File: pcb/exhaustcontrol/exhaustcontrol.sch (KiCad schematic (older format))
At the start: 17 parts, among them J1 Conn_01x03, J2 Conn_01x02, Q1 BC547, U1 74LS08

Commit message: Final fixes.
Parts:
- R1: value 5k6 -> 0R
- R2: value 1k -> 4k7
- U1: value 74LS08 -> 74HC08
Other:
- note added: "J7:5"
- note removed: "HEATER"
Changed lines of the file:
@@
 EESchema Schematic File Version 4
-LIBS:exhaustcontrol-cache
 EELAYER 30 0
 EELAYER END
@@
 P 2850 2600
 F 0 "U1" H 2850 2925 50  0000 C CNN
-F 1 "74LS08" H 2850 2834 50  0000 C CNN
+F 1 "74HC08" H 2850 2834 50  0000 C CNN
 F 2 "Package_DIP:DIP-14_W7.62mm_LongPads" H 2850 2600 50  0001 C CNN
 F 3 "http://www.ti.com/lit/gpn/sn74LS08" H 2850 2600 50  0001 C CNN
@@
 P 2300 2300
 F 0 "R1" H 2370 2346 50  0000 L CNN
-F 1 "5k6" H 2370 2255 50  0000 L CNN
+F 1 "0R" H 2370 2255 50  0000 L CNN
 F 2 "Resistor_THT:R_Axial_DIN0411_L9.9mm_D3.6mm_P12.70mm_Horizontal" V 2230 2300 50  0001 C CNN
 F 3 "~" H 2300 2300 50  0001 C CNN
@@
 P 2300 2900
 F 0 "R2" H 2370 2946 50  0000 L CNN
-F 1 "1k" H 2370 2855 50  0000 L CNN
+F 1 "4k7" H 2370 2855 50  0000 L CNN
 F 2 "Resistor_THT:R_Axial_DIN0411_L9.9mm_D3.6mm_P12.70mm_Horizontal" V 2230 2900 50  0001 C CNN
 F 3 "~" H 2300 2900 50  0001 C CNN
@@
 P 5300 2600
 F 0 "U1" H 5300 2925 50  0000 C CNN
-F 1 "74LS08" H 5300 2834 50  0000 C CNN
+F 1 "74HC08" H 5300 2834 50  0000 C CNN
 F 2 "Package_DIP:DIP-14_W7.62mm_LongPads" H 5300 2600 50  0001 C CNN
 F 3 "http://www.ti.com/lit/gpn/sn74LS08" H 5300 2600 50  0001 C CNN
@@
 P 5900 4850
 F 0 "U1" H 5900 5175 50  0000 C CNN
-F 1 "74LS08" H 5900 5084 50  0000 C CNN
+F 1 "74HC08" H 5900 5084 50  0000 C CNN
 F 2 "Package_DIP:DIP-14_W7.62mm_LongPads" H 5900 4850 50  0001 C CNN
 F 3 "http://www.ti.com/lit/gpn/sn74LS08" H 5900 4850 50  0001 C CNN
@@
 P 4550 4850
 F 0 "U1" H 4550 5175 50  0000 C CNN
-F 1 "74LS08" H 4550 5084 50  0000 C CNN
+F 1 "74HC08" H 4550 5084 50  0000 C CNN
 F 2 "Package_DIP:DIP-14_W7.62mm_LongPads" H 4550 4850 50  0001 C CNN
 F 3 "http://www.ti.com/lit/gpn/sn74LS08" H 4550 4850 50  0001 C CNN
@@
 +5V
 Text Notes 1150 2150 0    50   ~ 0
-HEATER
+J7:5
 Text Notes 1150 2300 0    50   ~ 0
 GND

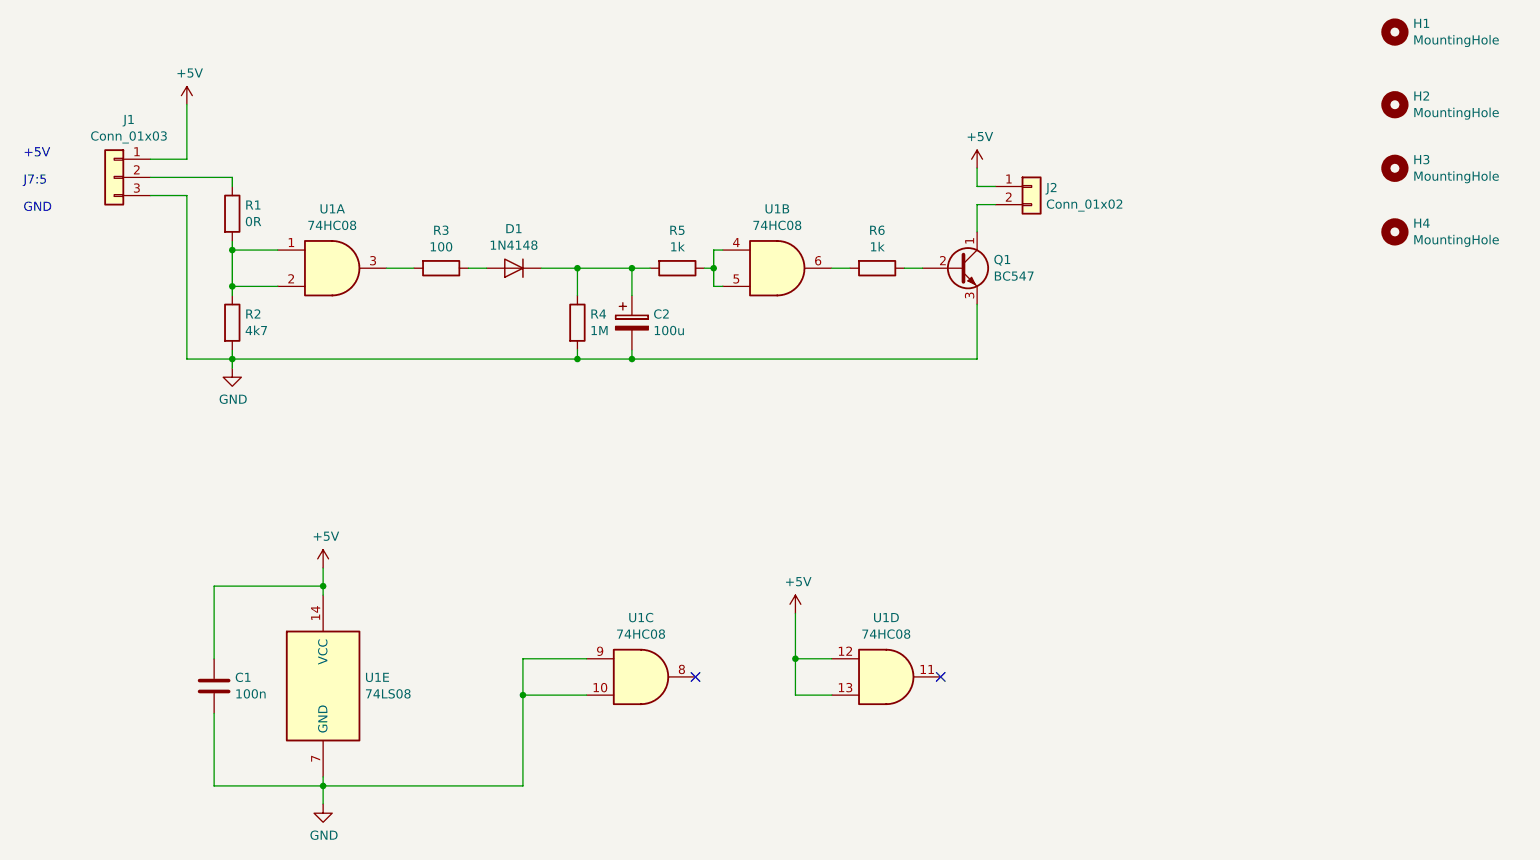
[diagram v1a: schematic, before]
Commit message: Run SSR off 24 V.
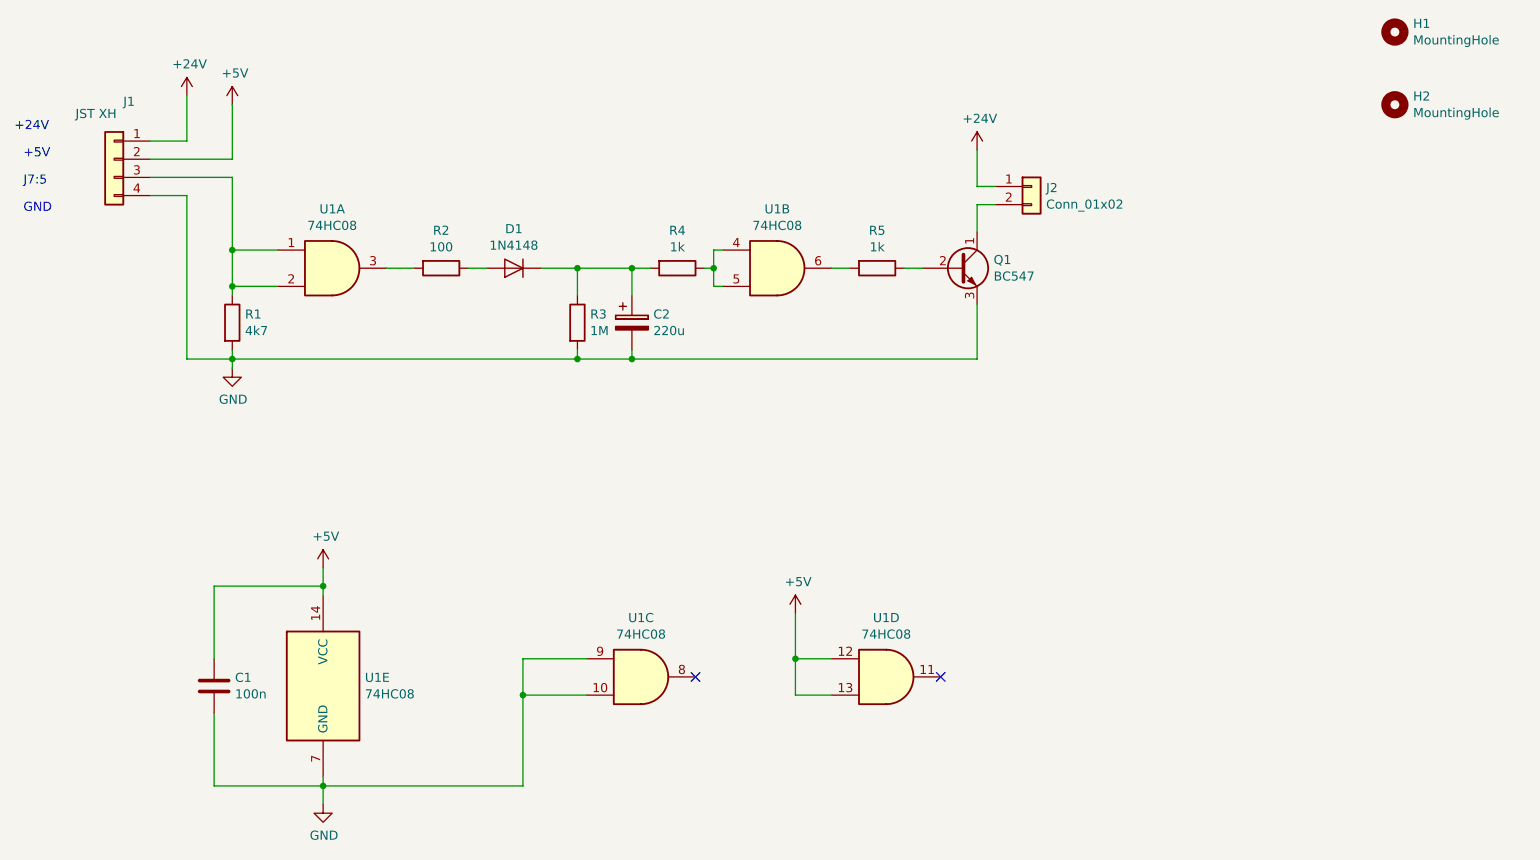
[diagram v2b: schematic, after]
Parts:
- removed H3, H4: MountingHole, MountingHole:MountingHole_3.2mm_M3, symbol Mechanical:MountingHole
- removed J1: Conn_01x03, Connector_JST:JST_XH_B03B-XH-A_1x03_P2.50mm_Vertical, symbol Connector_Generic:Conn_01x03
- removed R1: 0R, Resistor_THT:R_Axial_DIN0411_L9.9mm_D3.6mm_P12.70mm_Horizontal, symbol Device:R
- added J1: JST XH, Connector_JST:JST_XH_B04B-XH-A_1x04_P2.50mm_Vertical, symbol Connector_Generic:Conn_01x04
- C2: value 100u -> 220u
- U1: value 74LS08 -> 74HC08
- renumbered R2 to R1, R3 to R2, R4 to R3, R5 to R4, R6 to R5
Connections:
- net +5V: now also J1.2 (Pin_2); no longer J2.1 (Pin_1)
- net GND: now also J1.4 (Pin_4)
- net at R1.1, U1.1, U1.2: now also J1.3 (Pin_3)
- new net +24V: J1.1 (Pin_1), J2.1 (Pin_1)
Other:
- note added: "+24V"
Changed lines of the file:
@@
 $EndDescr
-$Comp
-L Connector_Generic:Conn_01x03 J1
-U 1 1 5DD1ACF4
-P 1650 2100
-F 0 "J1" H 1568 2417 50  0000 C CNN
-F 1 "Conn_01x03" H 1568 2326 50  0000 C CNN
-F 2 "Connector_JST:JST_XH_B03B-XH-A_1x03_P2.50mm_Vertical" H 1650 2100 50  0001 C CNN
-F 3 "~" H 1650 2100 50  0001 C CNN
-	1    1650 2100
-	-1   0    0    -1
-$EndComp
 $Comp
 L 74xx:74LS08 U1
@@
 $Comp
 L Device:R R1
-U 1 1 5DD1E131
-P 2300 2300
-F 0 "R1" H 2370 2346 50  0000 L CNN
-F 1 "0R" H 2370 2255 50  0000 L CNN
-F 2 "Resistor_THT:R_Axial_DIN0411_L9.9mm_D3.6mm_P12.70mm_Horizontal" V 2230 2300 50  0001 C CNN
-F 3 "~" H 2300 2300 50  0001 C CNN
-	1    2300 2300
-	1    0    0    -1
-$EndComp
-$Comp
-L Device:R R2
 U 1 1 5DD1E5FD
 P 2300 2900
-F 0 "R2" H 2370 2946 50  0000 L CNN
+F 0 "R1" H 2370 2946 50  0000 L CNN
 F 1 "4k7" H 2370 2855 50  0000 L CNN
 F 2 "Resistor_THT:R_Axial_DIN0411_L9.9mm_D3.6mm_P12.70mm_Horizontal" V 2230 2900 50  0001 C CNN
@@
 Connection ~ 2300 2500
 Wire Wire Line
-	2300 2500 2300 2450
-Wire Wire Line
 	2550 2700 2300 2700
 Connection ~ 2300 2700
@@
 	1850 2100 2300 2100
 Wire Wire Line
-	2300 2100 2300 2150
-Wire Wire Line
 	1850 2200 2050 2200
 Wire Wire Line
@@
 L power:+5V #PWR0102
 U 1 1 5DD1FC9C
-P 2050 1700
-F 0 "#PWR0102" H 2050 1550 50  0001 C CNN
-F 1 "+5V" H 2065 1873 50  0000 C CNN
-F 2 "" H 2050 1700 50  0001 C CNN
-F 3 "" H 2050 1700 50  0001 C CNN
-	1    2050 1700
-	1    0    0    -1
-$EndComp
-Wire Wire Line
-	2050 1700 2050 2000
-Wire Wire Line
-	2050 2000 1850 2000
-$Comp
-L Device:R R3
-U 1 1 5DD205AB
-P 3450 2600
-F 0 "R3" V 3243 2600 50  0000 C CNN
-F 1 "100" V 3334 2600 50  0000 C CNN
-F 2 "Resistor_THT:R_Axial_DIN0411_L9.9mm_D3.6mm_P12.70mm_Horizontal" V 3380 2600 50  0001 C CNN
-F 3 "~" H 3450 2600 50  0001 C CNN
-	1    3450 2600
-	0    1    1    0
+P 2300 1700
+F 0 "#PWR0102" H 2300 1550 50  0001 C CNN
+F 1 "+5V" H 2315 1873 50  0000 C CNN
+F 2 "" H 2300 1700 50  0001 C CNN
+F 3 "" H 2300 1700 50  0001 C CNN
+	1    2300 1700
+	1    0    0    -1
 $EndComp
 $Comp
@@
 $EndComp
 $Comp
-L Device:R R4
+L Device:R R3
 U 1 1 5DD20FF7
 P 4200 2900
-F 0 "R4" H 4270 2946 50  0000 L CNN
+F 0 "R3" H 4270 2946 50  0000 L CNN
 F 1 "1M" H 4270 2855 50  0000 L CNN
 F 2 "Resistor_THT:R_Axial_DIN0411_L9.9mm_D3.6mm_P12.70mm_Horizontal" V 4130 2900 50  0001 C CNN
@@
 P 4500 2900
 F 0 "C2" H 4618 2946 50  0000 L CNN
-F 1 "100u" H 4618 2855 50  0000 L CNN
+F 1 "220u" H 4618 2855 50  0000 L CNN
 F 2 "Capacitor_THT:CP_Radial_D10.0mm_P2.50mm_P5.00mm" H 4538 2750 50  0001 C CNN
 F 3 "~" H 4500 2900 50  0001 C CNN
@@
 $EndComp
 $Comp
-L Device:R R5
+L Device:R R4
 U 1 1 5DD21C09
 P 4750 2600
-F 0 "R5" V 4543 2600 50  0000 C CNN
+F 0 "R4" V 4543 2600 50  0000 C CNN
 F 1 "1k" V 4634 2600 50  0000 C CNN
 F 2 "Resistor_THT:R_Axial_DIN0411_L9.9mm_D3.6mm_P12.70mm_Horizontal" V 4680 2600 50  0001 C CNN
@@
 $EndComp
 $Comp
-L Device:R R6
+L Device:R R5
 U 1 1 5DD2E651
 P 5850 2600
-F 0 "R6" V 5643 2600 50  0000 C CNN
+F 0 "R5" V 5643 2600 50  0000 C CNN
 F 1 "1k" V 5734 2600 50  0000 C CNN
 F 2 "Resistor_THT:R_Axial_DIN0411_L9.9mm_D3.6mm_P12.70mm_Horizontal" V 5780 2600 50  0001 C CNN
@@
 Wire Wire Line
 	6400 2250 6400 2400
-$Comp
-L power:+5V #PWR0103
-U 1 1 5DD3100D
-P 6400 2050
-F 0 "#PWR0103" H 6400 1900 50  0001 C CNN
-F 1 "+5V" H 6415 2223 50  0000 C CNN
-F 2 "" H 6400 2050 50  0001 C CNN
-F 3 "" H 6400 2050 50  0001 C CNN
-	1    6400 2050
-	1    0    0    -1
-$EndComp
-Wire Wire Line
-	6400 2050 6400 2150
 Wire Wire Line
 	6400 2150 6500 2150
@@
 P 2800 4900
 F 0 "U1" H 3030 4946 50  0000 L CNN
-F 1 "74LS08" H 3030 4855 50  0000 L CNN
+F 1 "74HC08" H 3030 4855 50  0000 L CNN
 F 2 "Package_DIP:DIP-14_W7.62mm_LongPads" H 2800 4900 50  0001 C CNN
 F 3 "http://www.ti.com/lit/gpn/sn74LS08" H 2800 4900 50  0001 C CNN
@@
 $EndComp
 $Comp
-L Mechanical:MountingHole H3
-U 1 1 5DD5F4FD
-P 8700 2050
-F 0 "H3" H 8800 2096 50  0000 L CNN
-F 1 "MountingHole" H 8800 2005 50  0000 L CNN
-F 2 "MountingHole:MountingHole_3.2mm_M3" H 8700 2050 50  0001 C CNN
-F 3 "~" H 8700 2050 50  0001 C CNN
-	1    8700 2050
-	1    0    0    -1
-$EndComp
-$Comp
-L Mechanical:MountingHole H4
-U 1 1 5DD5FCF1
-P 8700 2400
-F 0 "H4" H 8800 2446 50  0000 L CNN
-F 1 "MountingHole" H 8800 2355 50  0000 L CNN
-F 2 "MountingHole:MountingHole_3.2mm_M3" H 8700 2400 50  0001 C CNN
-F 3 "~" H 8700 2400 50  0001 C CNN
-	1    8700 2400
-	1    0    0    -1
-$EndComp
+L Connector_Generic:Conn_01x04 J1
+U 1 1 5DEDA2B6
+P 1650 2000
+F 0 "J1" H 1568 2317 50  0000 C CNN
+F 1 "JST XH" H 1750 2250 50  0000 C CNN
+F 2 "Connector_JST:JST_XH_B04B-XH-A_1x04_P2.50mm_Vertical" H 1650 2000 50  0001 C CNN
+F 3 "~" H 1650 2000 50  0001 C CNN
+	1    1650 2000
+	-1   0    0    -1
+$EndComp
+Text Notes 1100 1850 0    50   ~ 0
++24V
+Wire Wire Line
+	2300 2000 2300 1700
+Wire Wire Line
+	1850 2000 2300 2000
+$Comp
+L power:+24V #PWR0103
+U 1 1 5DEE2714
+P 2050 1650
+F 0 "#PWR0103" H 2050 1500 50  0001 C CNN
+F 1 "+24V" H 2065 1823 50  0000 C CNN
+F 2 "" H 2050 1650 50  0001 C CNN
+F 3 "" H 2050 1650 50  0001 C CNN
+	1    2050 1650
+	1    0    0    -1
+$EndComp
+Wire Wire Line
+	2050 1650 2050 1900
+Wire Wire Line
+	2050 1900 1850 1900
+Wire Wire Line
+	2300 2100 2300 2500
+$Comp
+L Device:R R2
+U 1 1 5DD205AB
+P 3450 2600
+F 0 "R2" V 3243 2600 50  0000 C CNN
+F 1 "100" V 3334 2600 50  0000 C CNN
+F 2 "Resistor_THT:R_Axial_DIN0411_L9.9mm_D3.6mm_P12.70mm_Horizontal" V 3380 2600 50  0001 C CNN
+F 3 "~" H 3450 2600 50  0001 C CNN
+	1    3450 2600
+	0    1    1    0
+$EndComp
+$Comp
+L power:+24V #PWR0107
+U 1 1 5DEE7340
+P 6400 1950
+F 0 "#PWR0107" H 6400 1800 50  0001 C CNN
+F 1 "+24V" H 6415 2123 50  0000 C CNN
+F 2 "" H 6400 1950 50  0001 C CNN
+F 3 "" H 6400 1950 50  0001 C CNN
+	1    6400 1950
+	1    0    0    -1
+$EndComp
+Wire Wire Line
+	6400 1950 6400 2150
 $EndSCHEMATC
